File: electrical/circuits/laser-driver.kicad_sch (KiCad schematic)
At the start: 4 parts, among them Q1 IRLML2030TRPBF

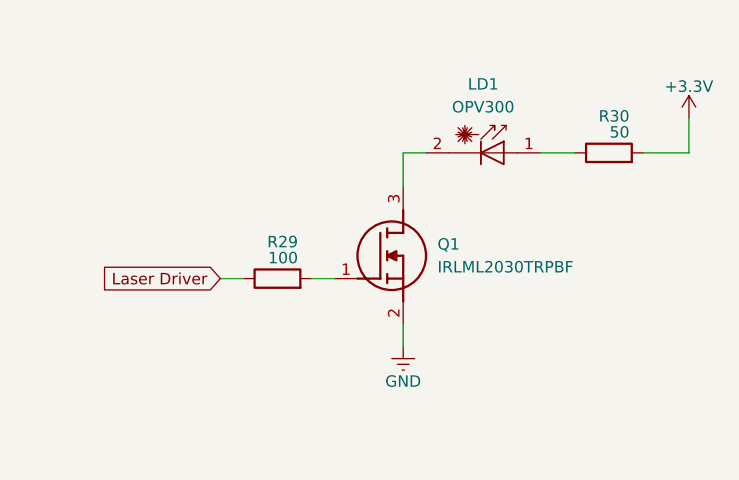
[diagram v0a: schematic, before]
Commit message: Added 10k pull-down resistor to laser driver MOSFET gate
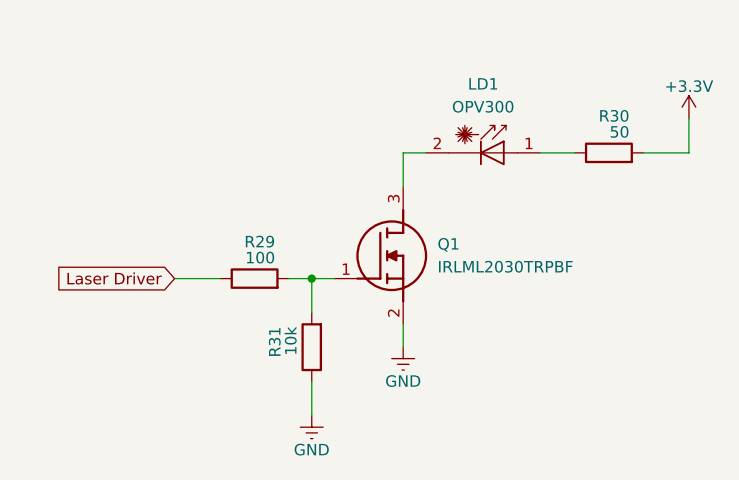
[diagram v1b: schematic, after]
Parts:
- added R31: 10k, symbol Device:R
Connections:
- net GND: now also R31.1
- net at Q1.1 (G), R29.2: now also R31.2
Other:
- moved on the sheet: R29
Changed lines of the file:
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@@
 		(date "2025-07-15")
 	)
+	(junction
+		(at 132.08 97.79)
+		(diameter 0)
+		(color 0 0 0 0)
+	)
 	(wire
 		(pts
@@
 	(wire
 		(pts
+			(xy 129.54 97.79) (xy 132.08 97.79)
+		)
+		(stroke
+			(width 0)
+			(type default)
+		)
+	)
+	(wire
+		(pts
+			(xy 157.48 83.82) (xy 161.29 83.82)
+		)
+		(stroke
+			(width 0)
+			(type default)
+		)
+	)
+	(wire
+		(pts
+			(xy 121.92 97.79) (xy 116.84 97.79)
+		)
+		(stroke
+			(width 0)
+			(type default)
+		)
+	)
+	(wire
+		(pts
+			(xy 173.99 80.01) (xy 173.99 83.82)
+		)
+		(stroke
+			(width 0)
+			(type default)
+		)
+	)
+	(wire
+		(pts
+			(xy 142.24 102.87) (xy 142.24 105.41)
+		)
+		(stroke
+			(width 0)
+			(type default)
+		)
+	)
+	(wire
+		(pts
+			(xy 132.08 97.79) (xy 132.08 101.6)
+		)
+		(stroke
+			(width 0)
+			(type default)
+		)
+	)
+	(wire
+		(pts
+			(xy 132.08 109.22) (xy 132.08 113.03)
+		)
+		(stroke
+			(width 0)
+			(type default)
+		)
+	)
+	(wire
+		(pts
+			(xy 144.78 83.82) (xy 142.24 83.82)
+		)
+		(stroke
+			(width 0)
+			(type default)
+		)
+	)
+	(wire
+		(pts
 			(xy 132.08 97.79) (xy 134.62 97.79)
-		)
-		(stroke
-			(width 0)
-			(type default)
-		)
-	)
-	(wire
-		(pts
-			(xy 157.48 83.82) (xy 161.29 83.82)
-		)
-		(stroke
-			(width 0)
-			(type default)
-		)
-	)
-	(wire
-		(pts
-			(xy 124.46 97.79) (xy 121.92 97.79)
-		)
-		(stroke
-			(width 0)
-			(type default)
-		)
-	)
-	(wire
-		(pts
-			(xy 173.99 80.01) (xy 173.99 83.82)
-		)
-		(stroke
-			(width 0)
-			(type default)
-		)
-	)
-	(wire
-		(pts
-			(xy 142.24 102.87) (xy 142.24 105.41)
-		)
-		(stroke
-			(width 0)
-			(type default)
-		)
-	)
-	(wire
-		(pts
-			(xy 144.78 83.82) (xy 142.24 83.82)
 		)
 		(stroke
@@
 	(global_label "Laser Driver"
 		(shape input)
-		(at 121.92 97.79 180)
+		(at 116.84 97.79 180)
 		(fields_autoplaced yes)
 		(effects
@@
 		)
 		(property "Intersheetrefs" "${INTERSHEET_REFS}"
-			(at 107.3838 97.79 0)
+			(at 102.3038 97.79 0)
 			(effects
 				(font
@@
 	)
 	(symbol
+		(lib_id "power:Earth")
+		(at 132.08 113.03 0)
+		(unit 1)
+		(exclude_from_sim no)
+		(in_bom yes)
+		(on_board yes)
+		(dnp no)
+		(property "Reference" "#PWR01"
+			(at 132.08 119.38 0)
+			(effects
+				(font
+					(size 1.27 1.27)
+				)
+				(hide yes)
+			)
+		)
+		(property "Value" "GND"
+			(at 132.08 116.84 0)
+			(effects
+				(font
+					(size 1.27 1.27)
+				)
+			)
+		)
+		(property "Footprint" ""
+			(at 132.08 113.03 0)
+			(effects
+				(font
+					(size 1.27 1.27)
+				)
+				(hide yes)
+			)
+		)
+		(property "Datasheet" "~"
+			(at 132.08 113.03 0)
+			(effects
+				(font
+					(size 1.27 1.27)
+				)
+				(hide yes)
+			)
+		)
+		(property "Description" "Power symbol creates a global label with name \"Earth\""
+			(at 132.08 113.03 0)
+			(effects
+				(font
+					(size 1.27 1.27)
+				)
+				(hide yes)
+			)
+		)
+		(pin "1"
+		)
+		(instances
+			(project "laser-driver"
+				(path "/a666a16b-400c-41db-93fb-73cda2564726"
+					(reference "#PWR01")
+					(unit 1)
+				)
+			)
+		)
+	)
+	(symbol
 		(lib_id "power:+3.3V")
 		(at 173.99 80.01 0)
@@
 	(symbol
 		(lib_id "Device:R")
-		(at 128.27 97.79 90)
+		(at 125.73 97.79 90)
 		(unit 1)
 		(exclude_from_sim no)
@@
 		(dnp no)
 		(property "Reference" "R29"
-			(at 130.556 93.726 90)
+			(at 128.016 93.726 90)
 			(effects
 				(font
@@
 		)
 		(property "Value" "100"
-			(at 130.556 95.504 90)
+			(at 128.016 95.504 90)
 			(effects
 				(font
@@
 		)
 		(property "Footprint" ""
-			(at 128.27 99.568 90)
+			(at 125.73 99.568 90)
 			(effects
 				(font
@@
 		)
 		(property "Datasheet" "~"
-			(at 128.27 97.79 0)
+			(at 125.73 97.79 0)
 			(effects
 				(font
@@
 		)
 		(property "Description" "Resistor"
-			(at 128.27 97.79 0)
+			(at 125.73 97.79 0)
 			(effects
 				(font
@@
 				(path "/5f57f40d-93c0-4665-857b-1def44fe2c31/7ec9df73-db03-4ceb-b23b-31f15c8bbf41"
 					(reference "R29")
+					(unit 1)
+				)
+			)
+		)
+	)
+	(symbol
+		(lib_id "Device:R")
+		(at 132.08 105.41 180)
+		(unit 1)
+		(exclude_from_sim no)
+		(in_bom yes)
+		(on_board yes)
+		(dnp no)
+		(property "Reference" "R31"
+			(at 128.016 103.124 90)
+			(effects
+				(font
+					(size 1.27 1.27)
+				)
+				(justify left)
+			)
+		)
+		(property "Value" "10k"
+			(at 129.794 103.124 90)
+			(effects
+				(font
+					(size 1.27 1.27)
+				)
+				(justify left)
+			)
+		)
+		(property "Footprint" ""
+			(at 133.858 105.41 90)
+			(effects
+				(font
+					(size 1.27 1.27)
+				)
+				(hide yes)
+			)
+		)
+		(property "Datasheet" "~"
+			(at 132.08 105.41 0)
+			(effects
+				(font
+					(size 1.27 1.27)
+				)
+				(hide yes)
+			)
+		)
+		(property "Description" "Resistor"
+			(at 132.08 105.41 0)
+			(effects
+				(font
+					(size 1.27 1.27)
+				)
+				(hide yes)
+			)
+		)
+		(pin "1"
+		)
+		(pin "2"
+		)
+		(instances
+			(project "laser-driver"
+				(path "/a666a16b-400c-41db-93fb-73cda2564726"
+					(reference "R31")
 					(unit 1)
 				)
@@
 		)
 	)
+	(sheet_instances
+		(path "/"
+			(page "1")
+		)
+	)

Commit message: Updated circuit schematics for 10BASE-T SNI mode
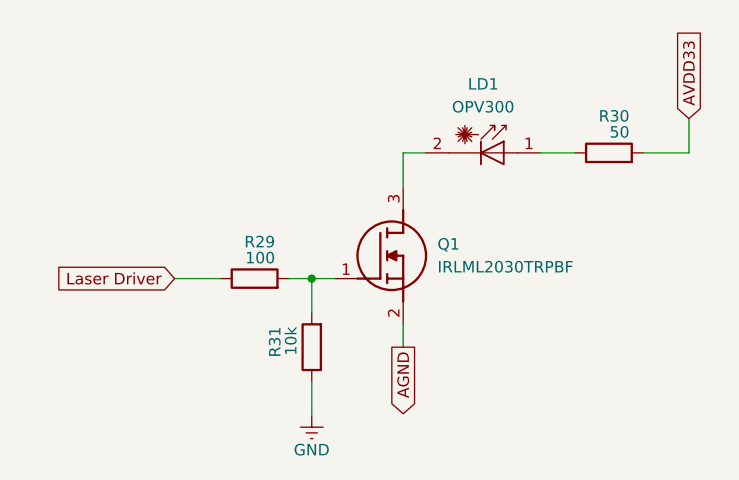
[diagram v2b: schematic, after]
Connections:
- net GND: no longer Q1.2 (S)
- net +3.3V renamed AVDD33
- new net AGND: Q1.2 (S)
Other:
- title: (none) -> Free Space Optical 10BASE-T Ethernet Transceiver Circuit
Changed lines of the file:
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@@
 	(paper "A")
 	(title_block
-		(date "2025-07-15")
+		(title "Free Space Optical 10BASE-T Ethernet Transceiver Circuit")
+		(date "2025-07-22")
 	)
 	(junction
@@
 			(width 0)
 			(type default)
+		)
+	)
+	(global_label "AGND"
+		(shape output)
+		(at 142.24 105.41 270)
+		(fields_autoplaced yes)
+		(effects
+			(font
+				(size 1.27 1.27)
+			)
+			(justify right)
+		)
+		(property "Intersheetrefs" "${INTERSHEET_REFS}"
+			(at 142.24 113.3543 90)
+			(effects
+				(font
+					(size 1.27 1.27)
+				)
+				(justify right)
+				(hide yes)
+			)
+		)
+	)
+	(global_label "AVDD33"
+		(shape input)
+		(at 173.99 80.01 90)
+		(fields_autoplaced yes)
+		(effects
+			(font
+				(size 1.27 1.27)
+			)
+			(justify left)
+		)
+		(property "Intersheetrefs" "${INTERSHEET_REFS}"
+			(at 173.99 69.8886 90)
+			(effects
+				(font
+					(size 1.27 1.27)
+				)
+				(justify left)
+				(hide yes)
+			)
 		)
 	)
@@
 					(unit 1)
 				)
-			)
-		)
-	)
-	(symbol
-		(lib_id "power:+3.3V")
-		(at 173.99 80.01 0)
-		(mirror y)
-		(unit 1)
-		(exclude_from_sim no)
-		(in_bom yes)
-		(on_board yes)
-		(dnp no)
-		(property "Reference" "#PWR041"
-			(at 173.99 83.82 0)
-			(effects
-				(font
-					(size 1.27 1.27)
-				)
-				(hide yes)
-			)
-		)
-		(property "Value" "+3.3V"
-			(at 173.99 76.454 0)
-			(effects
-				(font
-					(size 1.27 1.27)
-				)
-			)
-		)
-		(property "Footprint" ""
-			(at 173.99 80.01 0)
-			(effects
-				(font
-					(size 1.27 1.27)
-				)
-				(hide yes)
-			)
-		)
-		(property "Datasheet" ""
-			(at 173.99 80.01 0)
-			(effects
-				(font
-					(size 1.27 1.27)
-				)
-				(hide yes)
-			)
-		)
-		(property "Description" "Power symbol creates a global label with name \"+3.3V\""
-			(at 173.99 80.01 0)
-			(effects
-				(font
-					(size 1.27 1.27)
-				)
-				(hide yes)
-			)
-		)
-		(pin "1"
-		)
-		(instances
-			(project "FSOCom"
-				(path "/5f57f40d-93c0-4665-857b-1def44fe2c31/7ec9df73-db03-4ceb-b23b-31f15c8bbf41"
-					(reference "#PWR041")
-					(unit 1)
-				)
-			)
-		)
-	)
-	(symbol
-		(lib_id "power:Earth")
-		(at 142.24 105.41 0)
-		(unit 1)
-		(exclude_from_sim no)
-		(in_bom yes)
-		(on_board yes)
-		(dnp no)
-		(property "Reference" "#PWR040"
-			(at 142.24 111.76 0)
-			(effects
-				(font
-					(size 1.27 1.27)
-				)
-				(hide yes)
-			)
-		)
-		(property "Value" "GND"
-			(at 142.24 109.22 0)
-			(effects
-				(font
-					(size 1.27 1.27)
-				)
-			)
-		)
-		(property "Footprint" ""
-			(at 142.24 105.41 0)
-			(effects
-				(font
-					(size 1.27 1.27)
-				)
-				(hide yes)
-			)
-		)
-		(property "Datasheet" "~"
-			(at 142.24 105.41 0)
-			(effects
-				(font
-					(size 1.27 1.27)
-				)
-				(hide yes)
-			)
-		)
-		(property "Description" "Power symbol creates a global label with name \"Earth\""
-			(at 142.24 105.41 0)
-			(effects
-				(font
-					(size 1.27 1.27)
-				)
-				(hide yes)
-			)
-		)
-		(pin "1"
-		)
-		(instances
-			(project "FSOCom"
-				(path "/5f57f40d-93c0-4665-857b-1def44fe2c31/7ec9df73-db03-4ceb-b23b-31f15c8bbf41"
-					(reference "#PWR040")
-					(unit 1)
-				)
